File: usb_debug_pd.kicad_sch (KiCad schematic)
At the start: 84 parts, among them J7 Tag-Connect_TC2050-IDC-NL_2x5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, J8 USB-C_GCT_USB4105-GF-A, Q12 PJE138K, U29 W25Q80DV_USON, U30 TPS65988DHRSHR, U31 NTS0102_XSON, U32 NCP730BMT330_WSON, U34 FT230X_QFN, U40 AP22615A_TSOT26, U42 TPD4E05U06QDQARQ1

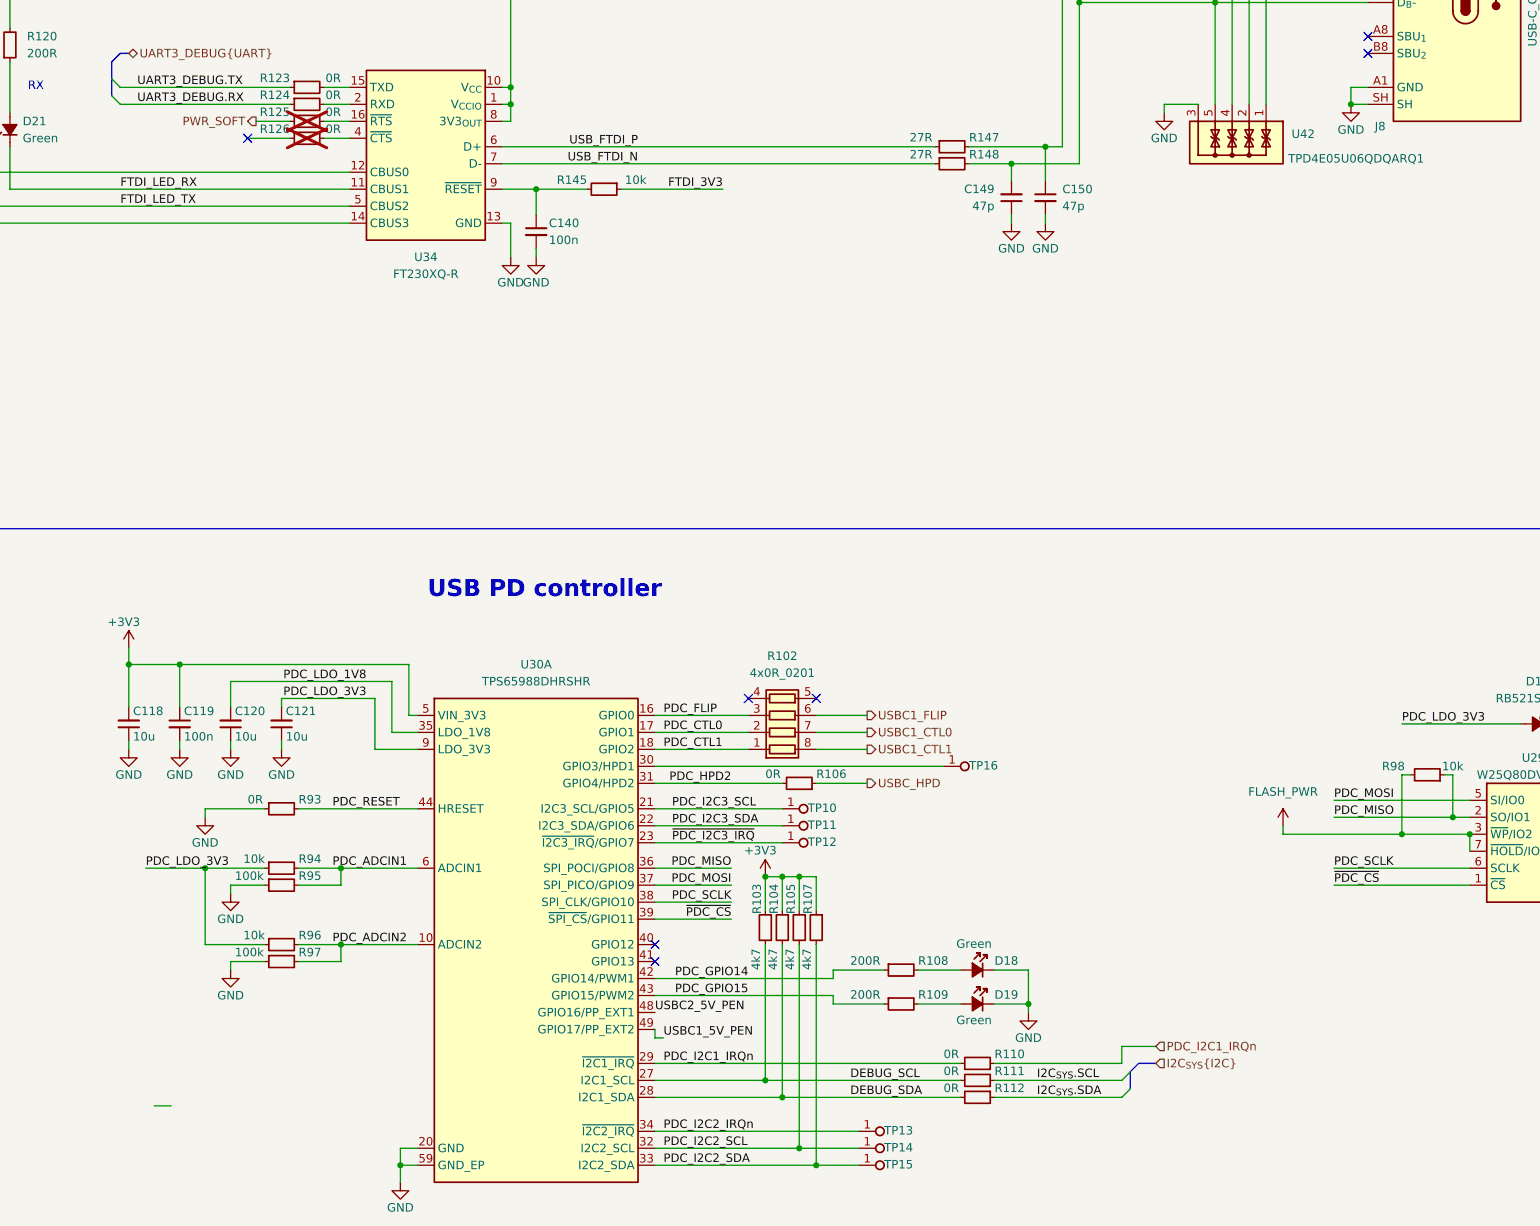
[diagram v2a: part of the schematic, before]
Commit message: [#82837] Add JTAG debug section to SoM_IO sheet. Delete SoM_Debug sheet and rearrange schematic pages
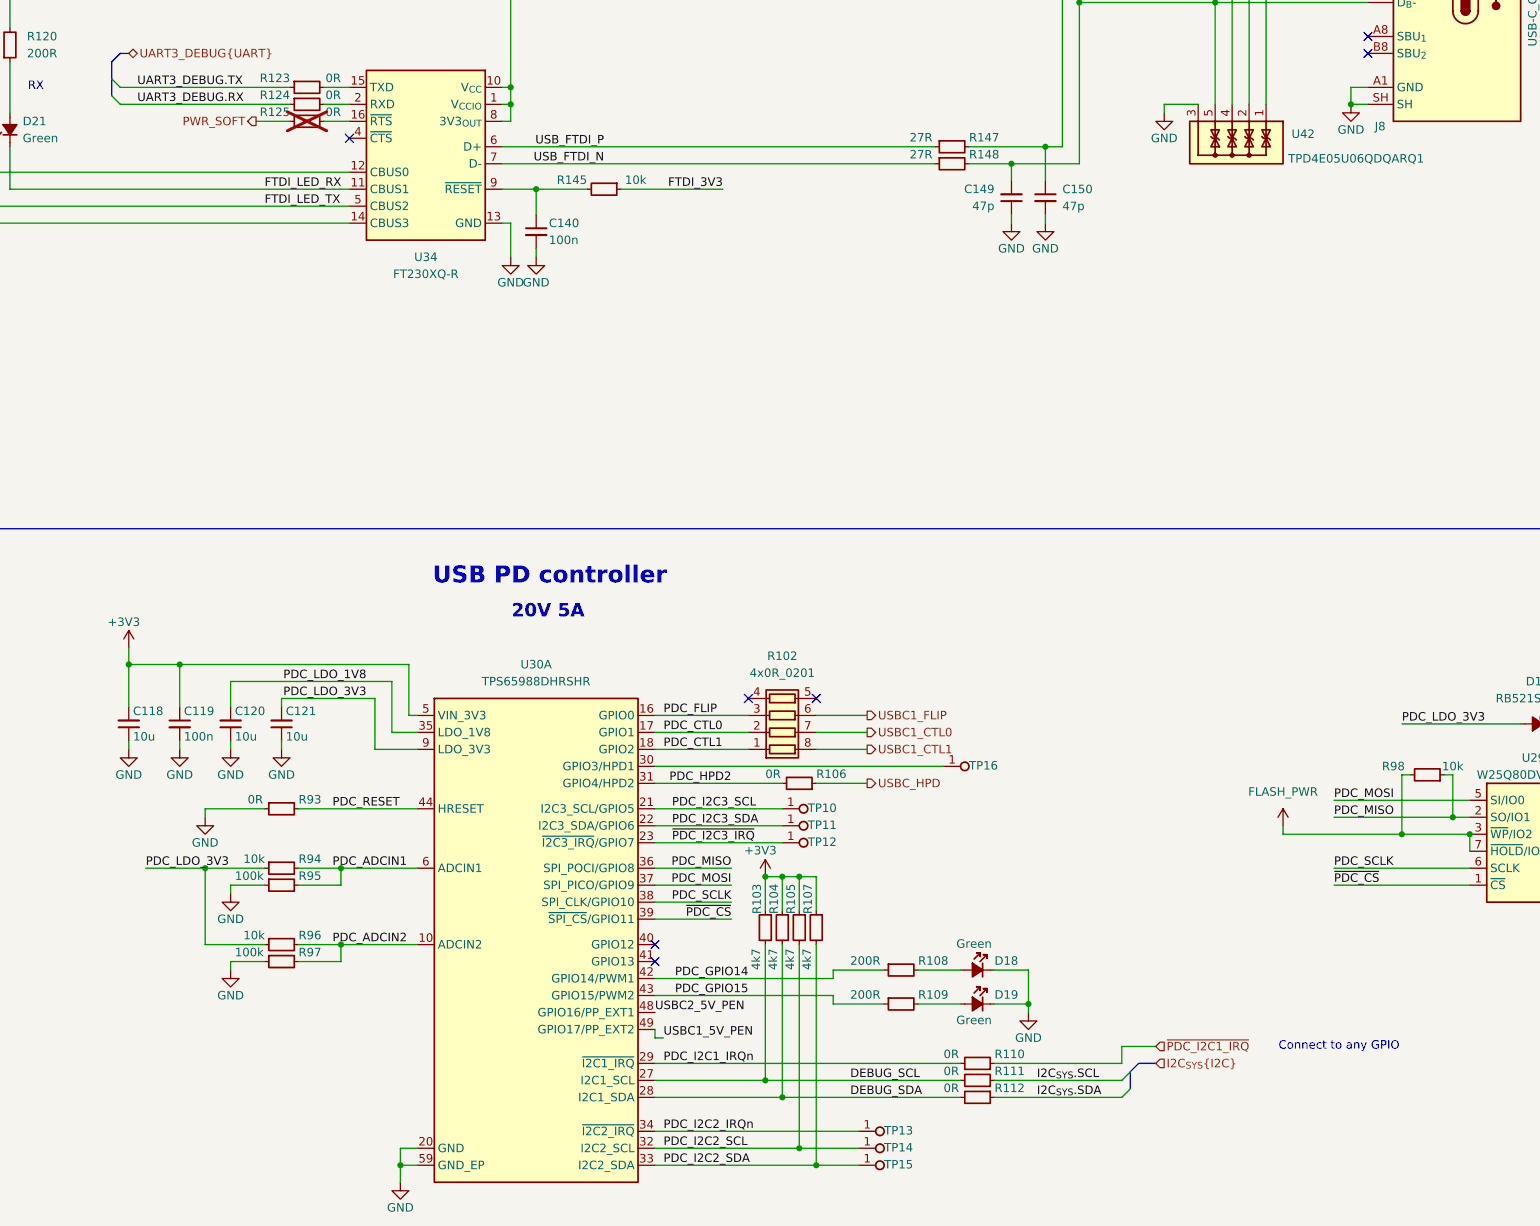
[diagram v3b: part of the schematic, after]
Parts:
- removed R126: R_0R_0402, antmicro-footprints:R_0402_1005Metric, symbol antmicroResistors0402:R_0R_0402
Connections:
- net PDC_I2C1_IRQn: no longer R110.1
- new net ~{PDC_I2C1_IRQ}: R110.1
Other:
- note added: "20V 5A"
- note added: "Connect to any GPIO"
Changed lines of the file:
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@@
 	(text "USB PD controller"
 		(exclude_from_sim no)
-		(at 200.66 174.244 0)
+		(at 201.422 172.212 0)
 		(effects
 			(font
@@
 		)
 	)
+	(text "Connect to any GPIO"
+		(exclude_from_sim no)
+		(at 319.532 242.57 0)
+		(effects
+			(font
+				(size 1.27 1.27)
+			)
+		)
+	)
 	(text "TX\n"
 		(exclude_from_sim no)
@@
 		)
 	)
+	(text "20V 5A"
+		(exclude_from_sim no)
+		(at 201.168 177.546 0)
+		(effects
+			(font
+				(size 2 2)
+				(thickness 0.4)
+				(bold yes)
+			)
+		)
+	)
 	(junction
 		(at 69.85 256.54)
@@
 	)
 	(no_connect
+		(at 171.45 106.68)
+	)
+	(no_connect
 		(at 217.17 227.33)
 	)
@@
 		(at 55.88 261.62)
 	)
-	(no_connect
-		(at 156.21 106.68)
-	)
 	(bus_entry
 		(at 288.29 248.92)
@@
 	(wire
 		(pts
-			(xy 142.24 251.46) (xy 144.78 251.46)
-		)
-		(stroke
-			(width 0)
-			(type default)
-		)
-	)
-	(wire
-		(pts
 			(xy 161.29 196.85) (xy 161.29 198.12)
 		)
@@
 	(wire
 		(pts
-			(xy 171.45 106.68) (xy 167.64 106.68)
-		)
-		(stroke
-			(width 0)
-			(type default)
-		)
-	)
-	(wire
-		(pts
 			(xy 256.54 231.14) (xy 262.89 231.14)
 		)
@@
 		)
 	)
-	(wire
-		(pts
-			(xy 162.56 106.68) (xy 156.21 106.68)
-		)
-		(stroke
-			(width 0)
-			(type default)
-		)
-	)
 	(bus
 		(pts
@@
 	)
 	(label "FTDI_LED_RX"
-		(at 137.16 114.3 0)
+		(at 158.75 114.3 0)
 		(effects
 			(font
@@
 	)
 	(label "USB_FTDI_P"
-		(at 214.63 107.95 180)
+		(at 209.55 107.95 180)
 		(effects
 			(font
@@
 	)
 	(label "USB_FTDI_N"
-		(at 214.63 110.49 180)
+		(at 209.55 110.49 180)
 		(effects
 			(font
@@
 	)
 	(label "FTDI_LED_TX"
-		(at 137.16 116.84 0)
+		(at 158.75 116.84 0)
 		(effects
 			(font
@@
 		)
 	)
-	(hierarchical_label "PDC_I2C1_IRQn"
+	(hierarchical_label "~{PDC_I2C1_IRQ}"
 		(shape input)
 		(at 292.1 242.57 0)
@@
 					(unit 1)
 				)
-			)
-		)
-	)
-	(symbol
-		(lib_name "R_0R_0402_9")
-		(lib_id "antmicroResistors0402:R_0R_0402")
-		(at 162.56 106.68 0)
-		(unit 1)
-		(exclude_from_sim no)
-		(in_bom no)
-		(on_board yes)
-		(dnp yes)
-		(property "Reference" "R126"
-			(at 162.56 106.045 0)
-			(effects
-				(font
-					(size 1.27 1.27)
-				)
-				(justify right bottom)
-			)
-		)
-		(property "Value" "R_0R_0402"
-			(at 182.88 119.38 0)
-			(effects
-				(font
-					(size 1.27 1.27)
-					(thickness 0.15)
-				)
-				(justify left bottom)
-				(hide yes)
-			)
-		)
-		(property "Footprint" "antmicro-footprints:R_0402_1005Metric"
-			(at 182.88 121.92 0)
-			(effects
-				(font
-					(size 1.27 1.27)
-					(thickness 0.15)
-				)
-				(justify left bottom)
-				(hide yes)
-			)
-		)
-		(property "Datasheet" "https://industrial.panasonic.com/cdbs/www-data/pdf/RDA0000/AOA0000C301.pdf"
-			(at 182.88 124.46 0)
-			(effects
-				(font
-					(size 1.27 1.27)
-					(thickness 0.15)
-				)
-				(justify left bottom)
-				(hide yes)
-			)
-		)
-		(property "Description" ""
-			(at 162.56 106.68 0)
-			(effects
-				(font
-					(size 1.27 1.27)
-				)
-				(hide yes)
-			)
-		)
-		(property "Manufacturer" "Panasonic"
-			(at 182.88 129.54 0)
-			(effects
-				(font
-					(size 1.27 1.27)
-					(thickness 0.15)
-				)
-				(justify left bottom)
-				(hide yes)
-			)
-		)
-		(property "MPN" "ERJ2GE0R00X"
-			(at 182.88 127 0)
-			(effects
-				(font
-					(size 1.27 1.27)
-					(thickness 0.15)
-				)
-				(justify left bottom)
-				(hide yes)
-			)
-		)
-		(property "Val" "0R"
-			(at 170.18 106.045 0)
-			(effects
-				(font
-					(size 1.27 1.27)
-					(thickness 0.15)
-				)
-				(justify right bottom)
-			)
-		)
-		(property "License" "Apache-2.0"
-			(at 182.88 132.08 0)
-			(effects
-				(font
-					(size 1.27 1.27)
-					(thickness 0.15)
-				)
-				(justify left bottom)
-				(hide yes)
-			)
-		)
-		(property "Author" "Antmicro"
-			(at 182.88 134.62 0)
-			(effects
-				(font
-					(size 1.27 1.27)
-					(thickness 0.15)
-				)
-				(justify left bottom)
-				(hide yes)
-			)
-		)
-		(property "Tolerance" "~"
-			(at 182.88 116.84 0)
-			(effects
-				(font
-					(size 1.27 1.27)
-				)
-				(justify left bottom)
-				(hide yes)
-			)
-		)
-		(property "Current" "1A"
-			(at 182.88 137.16 0)
-			(effects
-				(font
-					(size 1.27 1.27)
-					(thickness 0.15)
-				)
-				(justify left bottom)
-				(hide yes)
-			)
-		)
-		(pin "1"
-		)
-		(pin "2"
-		)
-		(instances
-			(project "jetson-agx-thor-baseboard"
-				(path "/f569b0be-0afd-48b7-93ee-28582a4c645c/12c19ba5-8fdc-4775-a33b-e8b1ade01b0a"
-					(reference "R126")
-					(unit 1)
-				)

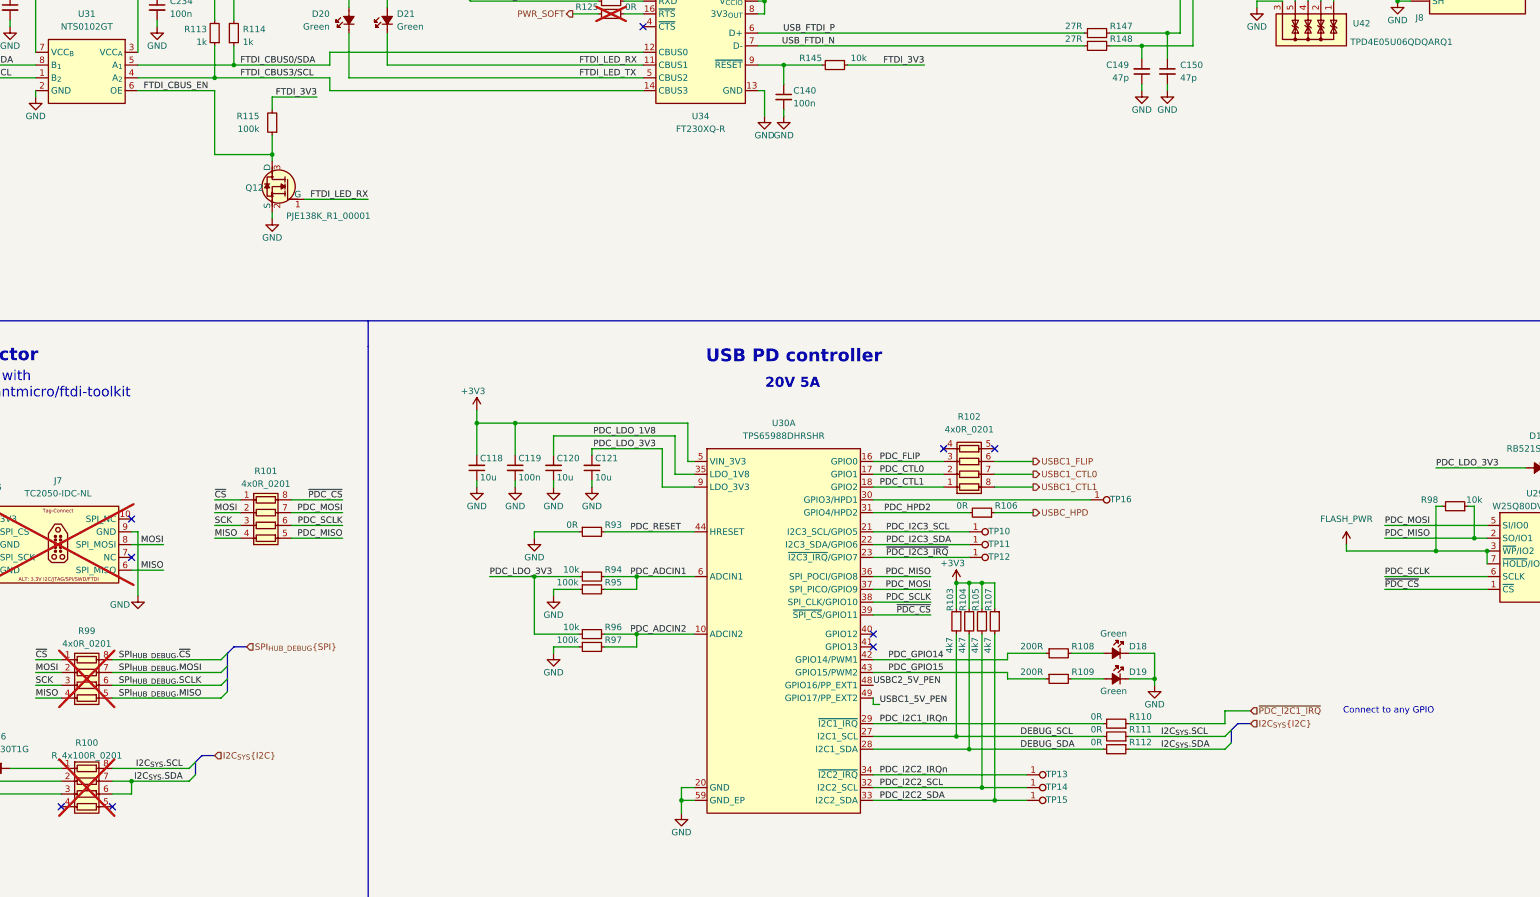
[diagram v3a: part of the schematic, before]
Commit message: [#82837] Prepare schematic to add root connections to USB section
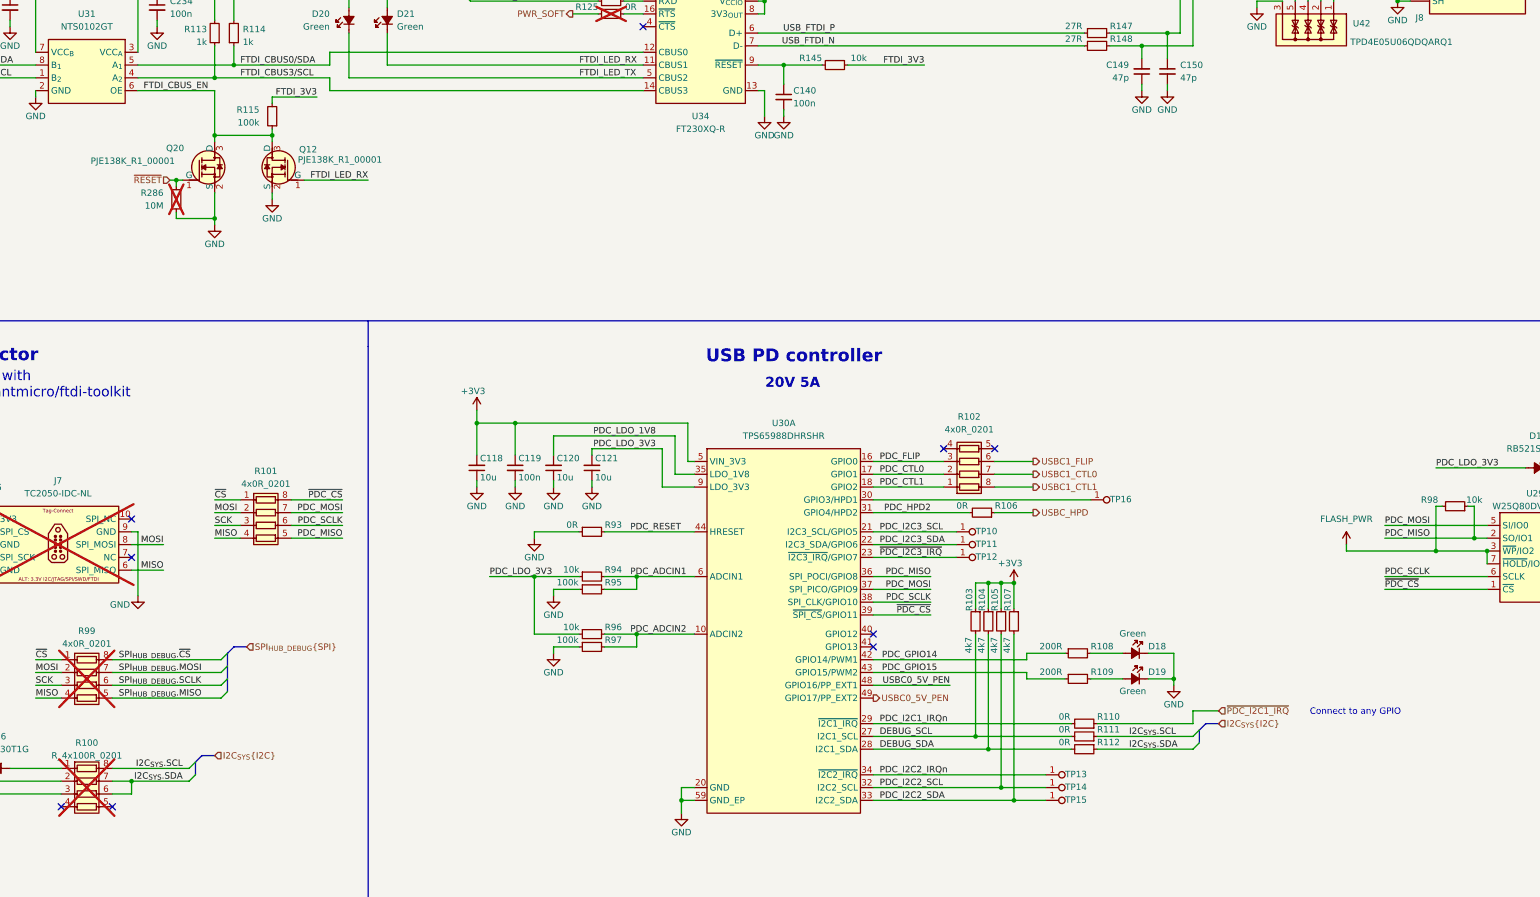
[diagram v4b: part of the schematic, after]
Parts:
- added Q20: PJE138K, antmicro-footprints:SOT-523, symbol antmicroTransistorsFETsMOSFETsSingle:PJE138K
- added R286: R_10M_0402, antmicro-footprints:R_0402_1005Metric, symbol antmicroResistors0402:R_10M_0402
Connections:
- net USBC1_5V_PEN is gone; now on net USBC0_5V_PEN: U30.49 (GPIO17/PP_EXT2)
- net USBC2_5V_PEN is gone; now on net USBC0_5V_PEN: U30.48 (GPIO16/PP_EXT1)
- net FTDI_CBUS_EN: now also Q20.3 (D)
- net GND: now also Q20.2 (S), R286.1
- new net ~{RESET}: Q20.1 (G), R286.2
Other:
- moved on the sheet: D18, D19, Q12, R103, R104, R105, R107, R108, R109, R110, R111, R112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

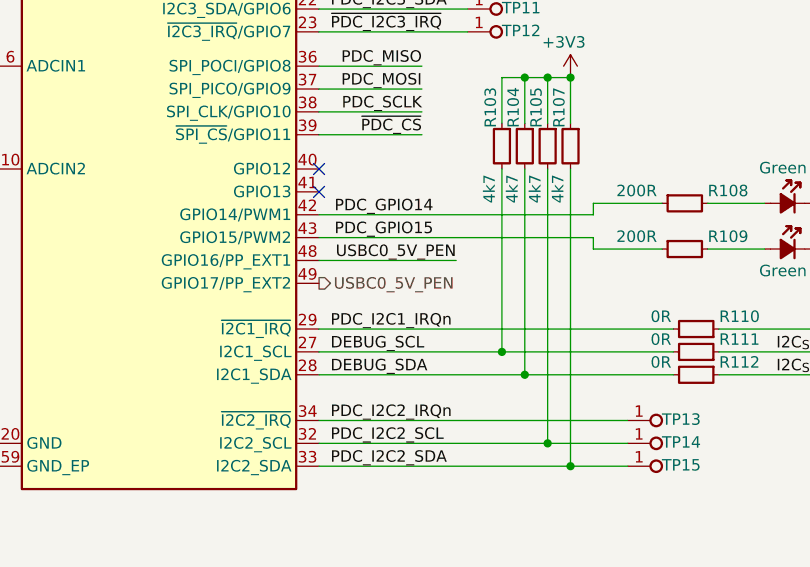
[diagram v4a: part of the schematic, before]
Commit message: [#82837] Finish mapping interfaces, waiting for new SoM symbol
[#82837] Add GPIO level shifter and route USB related GPIO on root
schematic

[#82837] WIP: Modify Power-up and reset section
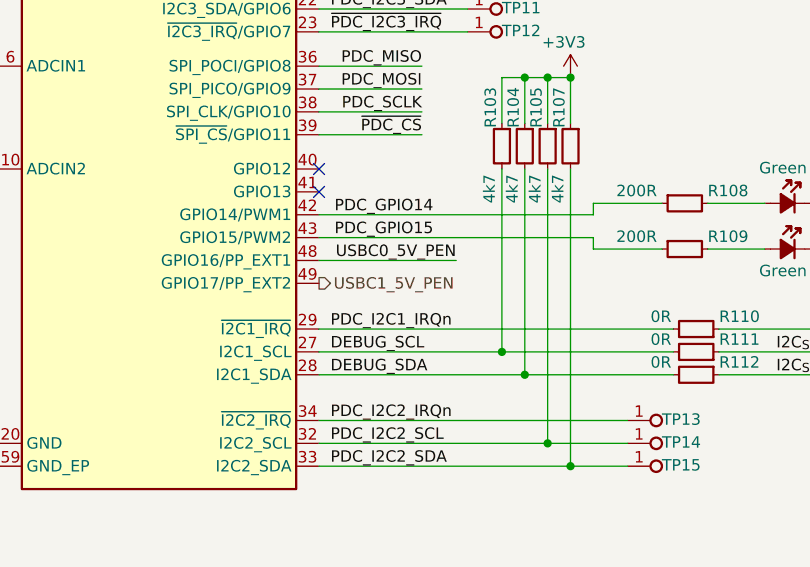
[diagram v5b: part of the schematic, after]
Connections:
- net USBC0_5V_PEN: no longer U30.49 (GPIO17/PP_EXT2)
- new net USBC1_5V_PEN: U30.49 (GPIO17/PP_EXT2)
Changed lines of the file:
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@@
 		)
 	)
-	(hierarchical_label "USBC0_5V_PEN"
+	(hierarchical_label "USBC1_5V_PEN"
 		(shape output)
 		(at 217.17 240.03 0)
